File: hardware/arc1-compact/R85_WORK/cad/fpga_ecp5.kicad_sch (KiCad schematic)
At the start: 101 parts, among them J5 ECP5 JTAG, J6 FPGA UART, U18 LFE5U-45F-6BG381C, U20 Schmitt, U21 iso SCK, U22 iso MOSI, U23 iso SS, U24 iso MISO, X1 25MHz

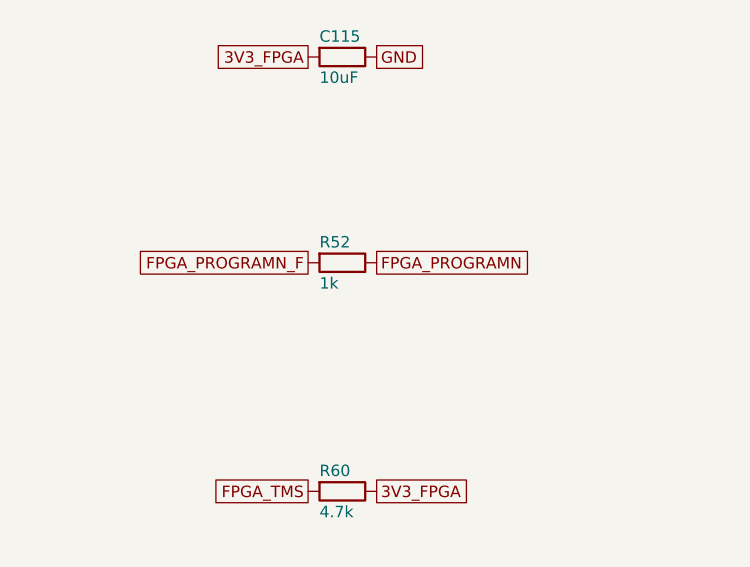
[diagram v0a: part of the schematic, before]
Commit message: ARC-1 Compact R8.5: STATUS_R85 (gates, HARD STOP options)
Co-Authored-By: Claude Opus 5.5 <noreply@anthropic.com>
Claude-Session: https://claude.ai/code/session_01UkiuLdbjDvK75uDzAPKsGs
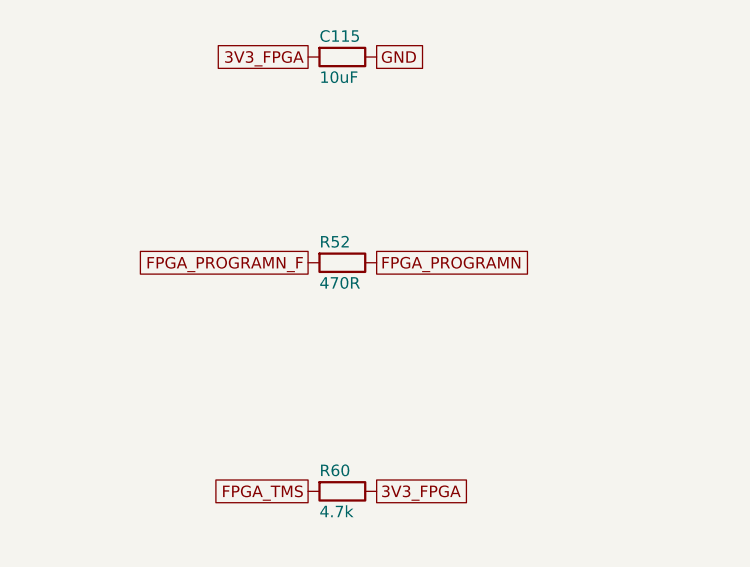
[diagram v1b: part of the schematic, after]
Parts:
- R52: value 1k -> 470R; Note F133 PE8 used open-drain (low or input only): calc 3.3*1k/5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 -> F133 PE8 used open-drain (low or input only): worst case 0.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
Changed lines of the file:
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@@
 (global_label "FPGA_PROGRAMN" (shape passive) (at 643.89 706.12 180) (fields_autoplaced yes) (effects (font (size 1.27 1.27)) (justify right)) (property "Intersheetrefs" "${INTERSHEET_REFS}" (at 643.89 706.12 0) (effects (font (size 1.27 1.27)) (hide yes))))
 (global_label "3V3_FPGA" (shape passive) (at 651.51 706.12 0) (fields_autoplaced yes) (effects (font (size 1.27 1.27)) (justify left)) (property "Intersheetrefs" "${INTERSHEET_REFS}" (at 651.51 706.12 0) (effects (font (size 1.27 1.27)) (hide yes))))
-(symbol (lib_id "ARC1_R85:R0402") (at 66.04 728.98 0) (unit 1) (exclude_from_sim no) (in_bom yes) (on_board yes) (dnp no) (property "Reference" "R52" (at 63.5 726.694 0) (effects (font (size 1.27 1.27)) (justify left))) (property "Value" "1k" (at 63.5 731.266 0) (effects (font (size 1.27 1.27)) (justify left))) (property "Footprint" "Resistor_SMD:R_0402_1005Metric" (at 66.04 728.98 0) (effects (font (size 1.27 1.27)) (hide yes))) (property "Datasheet" "" (at 66.04 728.98 0) (effects (font (size 1.27 1.27)) (hide yes))) (property "Description" "passive R0402" (at 66.04 728.98 0) (effects (font (size 1.27 1.27)) (hide yes))) (property "MPN" "" (at 66.04 728.98 0) (effects (font (size 1.27 1.27)) (hide yes))) (property "Manufacturer" "" (at 66.04 728.98 0) (effects (font (size 1.27 1.27)) (hide yes))) (property "LCSC" "" (at 66.04 728.98 0) (effects (font (size 1.27 1.27)) (hide yes))) (property "Evidence" "GENERIC_PASSIVE (value from design.py / analysis; MPN only where reused from SLIM4 R26 BOM)" (at 66.04 728.98 0) (effects (font (size 1.27 1.27)) (hide yes))) (property "Footprint_status" "STD_LIB" (at 66.04 728.98 0) (effects (font (size 1.27 1.27)) (hide yes))) (property "Note" "F133 PE8 used open-drain (low or input only): calc 3.3*1k/5.7k = 0.58 V < VIL 0.8 V" (at 66.04 728.98 0) (effects (font (size 1.27 1.27)) (hide yes))) (property "Source" "generic two-terminal" (at 66.04 728.98 0) (effects (font (size 1.27 1.27)) (hide yes))) (property "Reuse" "" (at 66.04 728.98 0) (effects (font (size 1.27 1.27)) (hide yes))) (pin "1") (pin "2") (instances (project "ARC1_R85" (path "/493c9a78-7bcd-5ad8-9af7-e69344718a5f/69914ada-66e1-551b-9740-3f2ff0659949" (reference "R52") (unit 1)))) )
+(symbol (lib_id "ARC1_R85:R0402") (at 66.04 728.98 0) (unit 1) (exclude_from_sim no) (in_bom yes) (on_board yes) (dnp no) (property "Reference" "R52" (at 63.5 726.694 0) (effects (font (size 1.27 1.27)) (justify left))) (property "Value" "470R" (at 63.5 731.266 0) (effects (font (size 1.27 1.27)) (justify left))) (property "Footprint" "Resistor_SMD:R_0402_1005Metric" (at 66.04 728.98 0) (effects (font (size 1.27 1.27)) (hide yes))) (property "Datasheet" "" (at 66.04 728.98 0) (effects (font (size 1.27 1.27)) (hide yes))) (property "Description" "passive R0402" (at 66.04 728.98 0) (effects (font (size 1.27 1.27)) (hide yes))) (property "MPN" "" (at 66.04 728.98 0) (effects (font (size 1.27 1.27)) (hide yes))) (property "Manufacturer" "" (at 66.04 728.98 0) (effects (font (size 1.27 1.27)) (hide yes))) (property "LCSC" "" (at 66.04 728.98 0) (effects (font (size 1.27 1.27)) (hide yes))) (property "Evidence" "GENERIC_PASSIVE (value from design.py / analysis; MPN only where reused from SLIM4 R26 BOM)" (at 66.04 728.98 0) (effects (font (size 1.27 1.27)) (hide yes))) (property "Footprint_status" "STD_LIB" (at 66.04 728.98 0) (effects (font (size 1.27 1.27)) (hide yes))) (property "Note" "F133 PE8 used open-drain (low or input only): worst case 0.50 V < VIL 0.8 V (analysis/electrical_margins_r85.py)" (at 66.04 728.98 0) (effects (font (size 1.27 1.27)) (hide yes))) (property "Source" "generic two-terminal" (at 66.04 728.98 0) (effects (font (size 1.27 1.27)) (hide yes))) (property "Reuse" "" (at 66.04 728.98 0) (effects (font (size 1.27 1.27)) (hide yes))) (pin "1") (pin "2") (instances (project "ARC1_R85" (path "/493c9a78-7bcd-5ad8-9af7-e69344718a5f/69914ada-66e1-551b-9740-3f2ff0659949" (reference "R52") (unit 1)))) )
 (global_label "FPGA_PROGRAMN_F" (shape passive) (at 62.23 728.98 180) (fields_autoplaced yes) (effects (font (size 1.27 1.27)) (justify right)) (property "Intersheetrefs" "${INTERSHEET_REFS}" (at 62.23 728.98 0) (effects (font (size 1.27 1.27)) (hide yes))))
 (global_label "FPGA_PROGRAMN" (shape passive) (at 69.85 728.98 0) (fields_autoplaced yes) (effects (font (size 1.27 1.27)) (justify left)) (property "Intersheetrefs" "${INTERSHEET_REFS}" (at 69.85 728.98 0) (effects (font (size 1.27 1.27)) (hide yes))))
